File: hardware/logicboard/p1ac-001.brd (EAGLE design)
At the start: 95 x 72 mm, 30 parts, among them IC1 74LS595N, IC2 74LS595N, K1 AQG12105, K10 AQG12105, K11 AQG12105, K12 AQG12105, K13 AQG12105, K14 AQG12105, K15 AQG12105, K16 AQG12105, K2 AQG12105, K3 AQG12105, K4 AQG12105, K5 AQG12105, K6 AQG12105, K7 AQG12105, K8 AQG12105, K9 AQG12105

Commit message: First shot.
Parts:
- removed IC2: 74LS595N, 74xx-us:DIL16
- removed K10, K11, K12, K13, K14, K15, K16, K9: AQG12105, relay:AQG
- removed SV1: (no value), con-ml:ML34L
- removed ULN2: (no value), SparkFun-IC-Special-Function:DIL18
- added DZ1: LB10, led:LB10
- added J2, J3, J4, J5, J6, J7, J8, J9: (no value), SparkFun-Connectors:MOLEX-1X2
- added RN1: (no value), resistor-dil:DIL16
- J1: device Seeed-Connector:3P-L14.2*W11.0*H9.0MM -> SparkFun-Connectors:MOLEX-1X2
- moved K8 33.0 mm to (78.0, 43.0)
- moved K7 29.0 mm to (69.0, 43.0)
- moved K6 26.0 mm to (61.0, 43.0)
- moved K5 17.0 mm to (47.0, 43.0)
- moved K4 13.0 mm to (36.0, 43.0)
- moved K3 8.00 mm to (26.0, 43.0)
- moved J1 7.81 mm to (21.0, 66.0), turned to 0 degrees
- moved K2 6.00 mm to (19.0, 43.0)
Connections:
- net S1 renamed Q1
- net S2 renamed Q2
- net S3 renamed Q3
- net S4 renamed Q4
- net S6 renamed Q6
- net S7 renamed Q7
- net S8 renamed Q8
- removed net +24V: J1.+, K1.O2, K10.O2, K11.O2, K12.O2, K13.O2, K14.O2, K15.O2, K16.O2, K2.O2, K3.O2, K4.O2, K5.O2, K6.O2, K7.O2, K8.O2, K9.O2
- removed net N$9: IC1.9, IC2.14
- removed net R10: K10.-, ULN2.17
- removed net R11: K11.-, ULN2.16
- removed net R12: K12.-, ULN2.15
- removed net R13: K13.-, ULN2.14
- removed net R14: K14.-, ULN2.13
- removed net R15: K15.-, ULN2.12
- removed net R16: K16.-, ULN2.11
- removed net R9: K9.-, ULN2.18
- removed net S10: IC2.1, ULN2.2
- removed net S11: IC2.2, ULN2.3
- removed net S12: IC2.3, ULN2.4
- removed net S13: IC2.4, ULN2.5
- removed net S14: IC2.5, ULN2.6
- removed net S15: IC2.6, ULN2.7
- removed net S16: IC2.7, ULN2.8
- removed net S9: IC2.15, ULN2.1
- removed net X10: K10.O1, SV1.19
- removed net X11: K11.O1, SV1.21
- removed net X12: K12.O1, SV1.23
- removed net X13: K13.O1, SV1.25
- removed net X14: K14.O1, SV1.27
- removed net X15: K15.O1, SV1.29
- removed net X16: K16.O1, SV1.31
- removed net X9: K9.O1, SV1.17
- new net AC1: J9.1, K1.O2, K2.O2, K3.O2, K4.O2, K5.O2, K6.O2, K7.O2, K8.O2
- new net AC2: J1.2, J2.2, J3.2, J4.2, J5.2, J6.2, J7.2, J8.2, J9.2
- new net N$1: IC1.9
- new net N$2: DZ1.1, RN1.16
- new net Q5: ULN1.5
- net CLR: no longer IC2.10
- net GND: no longer IC2.13, IC2.8, J1.-1, J1.-2, SV1.10, SV1.12, SV1.14, SV1.16, SV1.18, SV1.2, SV1.20, SV1.22, SV1.24, SV1.26, SV1.28, SV1.30, SV1.32, SV1.33, SV1.34, SV1.4, SV1.6, SV1.8, ULN2.9
- net R1: now also DZ1.20
- net RCLK: no longer IC2.12
- net S5: no longer ULN1.5
- net SCLK: no longer IC2.11
- net SOUT: no longer IC2.9
- net VCC: now also RN1.1; no longer IC2.16, K10.+, K11.+, K12.+, K13.+, K14.+, K15.+, K16.+, K9.+, ULN2.10
- net X1: now also J1.1; no longer SV1.1
- net X2: now also J2.1; no longer SV1.3
- net X3: now also J3.1; no longer SV1.5
- net X4: now also J4.1; no longer SV1.7
- net X5: now also J5.1; no longer SV1.9
- net X6: now also J6.1; no longer SV1.11
- net X7: now also J7.1; no longer SV1.13
- net X8: now also J8.1; no longer SV1.15
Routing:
- net GND: track 280.0 -> 0.00 mm, vias 1 -> 0
- net VCC: track 195.9 -> 0.00 mm
- net SCLK: track 93.9 -> 0.00 mm, vias 1 -> 0
- net CLR: track 92.1 -> 0.00 mm, vias 1 -> 0
- net RCLK: track 90.5 -> 0.00 mm
- net +24V: track 85.9 -> 0.00 mm
- net Q3: track 46.5 -> 0.00 mm
- net S14: track 42.2 -> 0.00 mm
- net S5: track 40.6 -> 0.00 mm
- net S11: track 40.1 -> 0.00 mm
- net Q2: track 39.1 -> 0.00 mm
- net S12: track 37.3 -> 0.00 mm
- net N$9: track 36.2 -> 0.00 mm
- net SIN: track 34.6 -> 0.00 mm
- net S10: track 30.1 -> 0.00 mm
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- removed copper zone on layer 1, net GND
- removed copper zone on layer 16, net GND

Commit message: Working.
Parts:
- moved J8 49.1 mm to (77.0, 69.0), turned to 180 degrees
- moved J2 42.1 mm to (29.0, 69.0), turned to 180 degrees
- moved J7 35.1 mm to (69.0, 69.0), turned to 180 degrees
- moved J3 27.2 mm to (37.0, 69.0), turned to 180 degrees
- moved J6 19.2 mm to (61.0, 69.0), turned to 180 degrees
- moved K1 13.9 mm to (21.0, 48.0)
- moved J9 12.7 mm to (13.0, 69.0), turned to 180 degrees
- moved K3 12.1 mm to (37.0, 48.0)
- moved J4 11.4 mm to (45.0, 69.0), turned to 180 degrees
- moved K2 11.2 mm to (29.0, 48.0)
- moved K4 10.3 mm to (45.0, 48.0)
- moved K5 7.81 mm to (53.0, 48.0)
- moved K8 5.10 mm to (77.0, 48.0)
- moved J5 5.00 mm to (53.0, 69.0), turned to 180 degrees
- moved K6 5.00 mm to (61.0, 48.0)
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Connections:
- removed net N$1: IC1.9
- removed net S5: IC1.4
- new net N$10: DZ1.4, RN1.13
- new net N$13: DZ1.5, RN1.12
- new net N$16: DZ1.6, RN1.11
- new net N$19: DZ1.7, RN1.10
- new net N$22: DZ1.8, RN1.9
- new net N$4: DZ1.2, RN1.15
- new net N$7: DZ1.3, RN1.14
- net Q5: now also IC1.4
- net R2: now also DZ1.19
- net R3: now also DZ1.18
- net R4: now also DZ1.17
- net R5: now also DZ1.16
- net R6: now also DZ1.15
- net R7: now also DZ1.14
- net R8: now also DZ1.13
- net SOUT: now also IC1.9
- net VCC: now also RN1.2, RN1.3, RN1.4, RN1.5, RN1.6, RN1.7, RN1.8
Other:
- board text added: "AC100V"
- board text added: "Pineapple I ac 1.0.0-X"
- board text removed: "DC24V2A"
- board text removed: "No."
- board text removed: "Pineapple 128 Relay Unit 1.0.0-X"

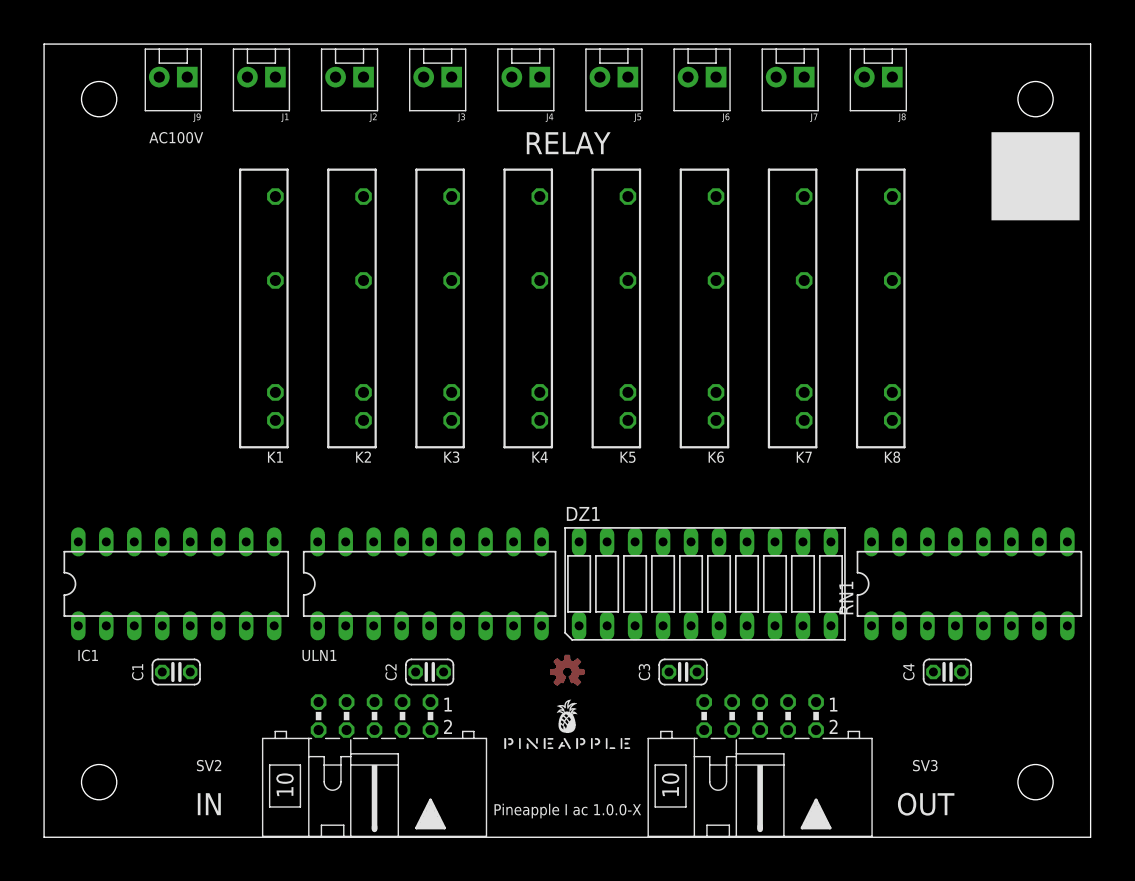
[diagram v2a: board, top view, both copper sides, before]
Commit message: Board design of Pineapple I ac driver.
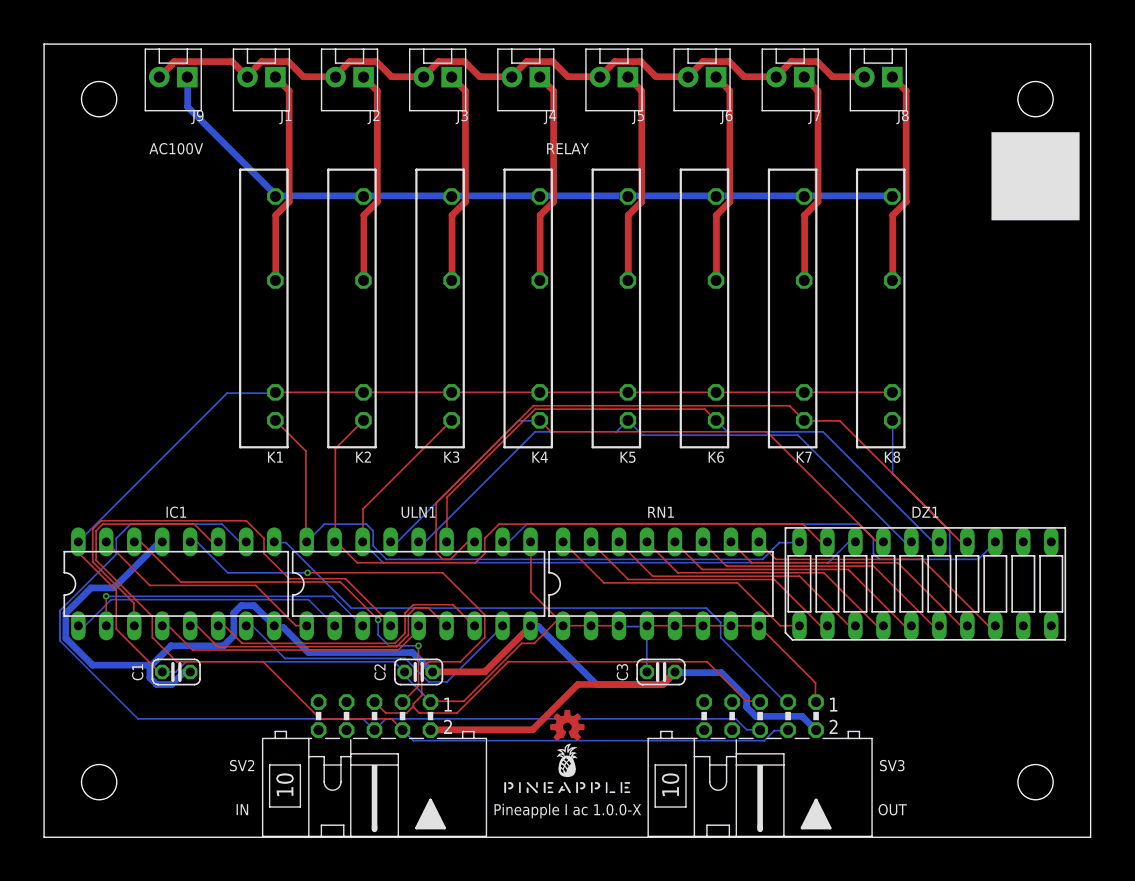
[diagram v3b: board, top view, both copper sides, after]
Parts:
- removed C4: (no value), resistor:C025-024X044
- moved RN1 28.0 mm to (56.0, 23.0)
- moved DZ1 20.0 mm to (80.0, 23.0)
- moved LOGO1 5.00 mm to (47.5, 10.0)
- moved U$1 4.00 mm to (47.5, 4.00)
- moved C3 2.00 mm to (56.0, 15.0)
- moved C2 1.00 mm to (34.0, 15.0)
- moved ULN1 1.00 mm to (34.0, 23.0)
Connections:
- net GND: no longer C4.2
- net VCC: no longer C4.1
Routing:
- net VCC: track 0.00 -> 176.5 mm
- net GND: track 0.00 -> 125.7 mm
- net CLR: track 0.00 -> 92.2 mm
- net SCLK: track 0.00 -> 85.8 mm
- net RCLK: track 0.00 -> 81.6 mm, vias 0 -> 1
- net AC2: track 0.00 -> 73.6 mm
- net AC1: track 0.00 -> 70.4 mm
- net R7: track 0.00 -> 65.9 mm
- net R8: track 0.00 -> 63.0 mm
- net R3: track 0.00 -> 60.7 mm
- net R2: track 0.00 -> 60.6 mm
- net R1: track 0.00 -> 60.4 mm
- net R6: track 0.00 -> 57.1 mm
- net R4: track 0.00 -> 53.9 mm
- net R5: track 0.00 -> 53.9 mm
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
